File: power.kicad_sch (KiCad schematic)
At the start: 13 parts, among them J2 USB_B_Micro, U2 AP2112K-3.3TRG1, U3 MCP73831T-2ACI/OT

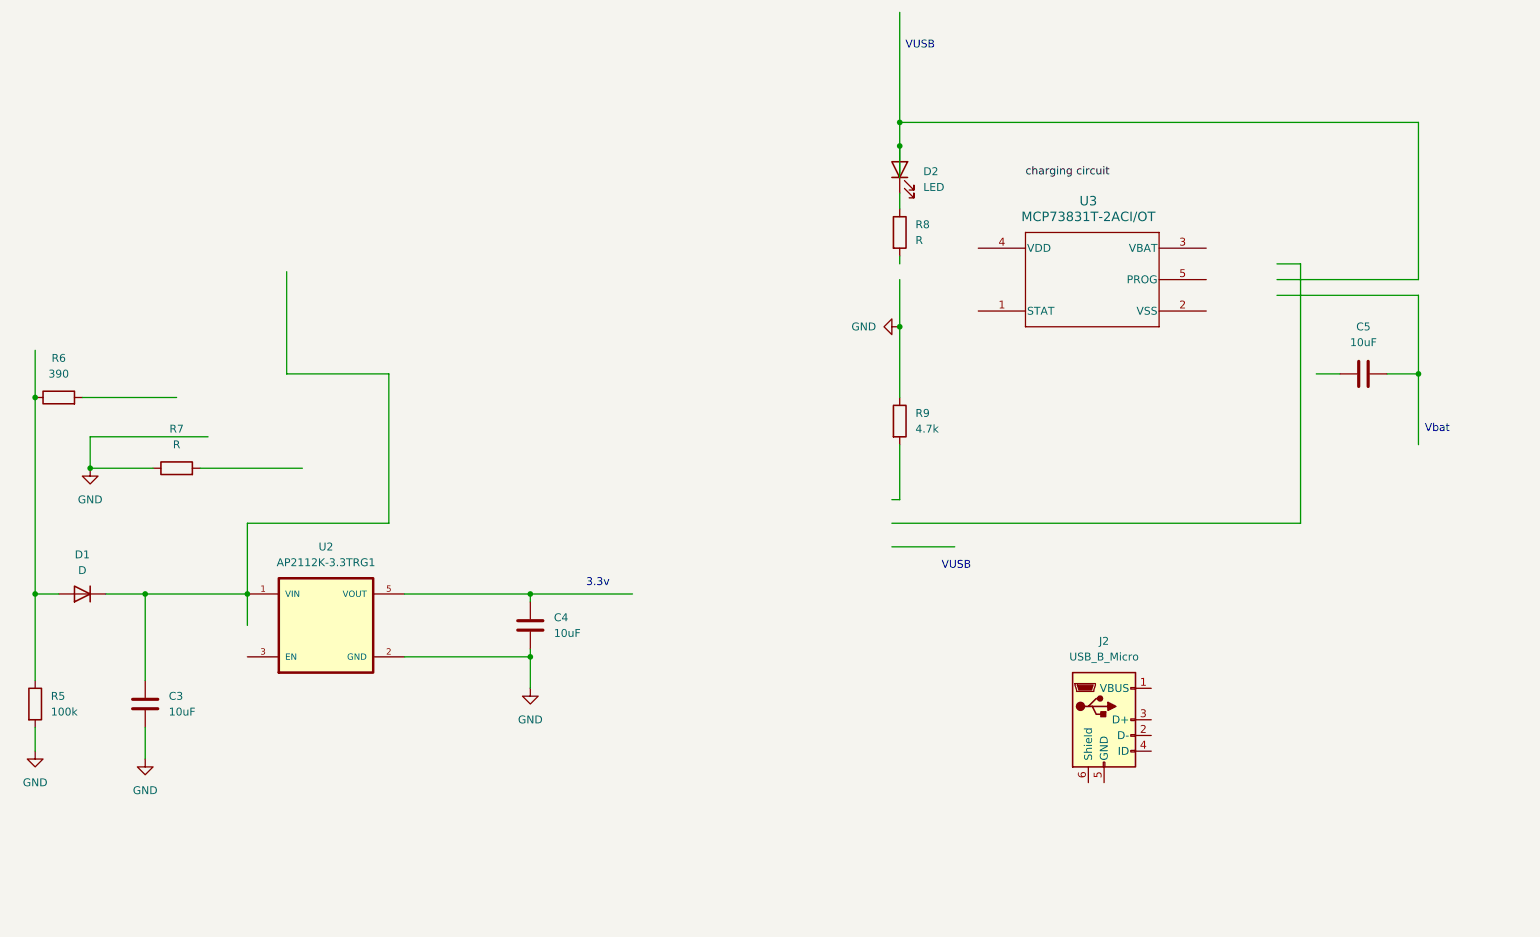
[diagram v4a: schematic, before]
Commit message: update power supply
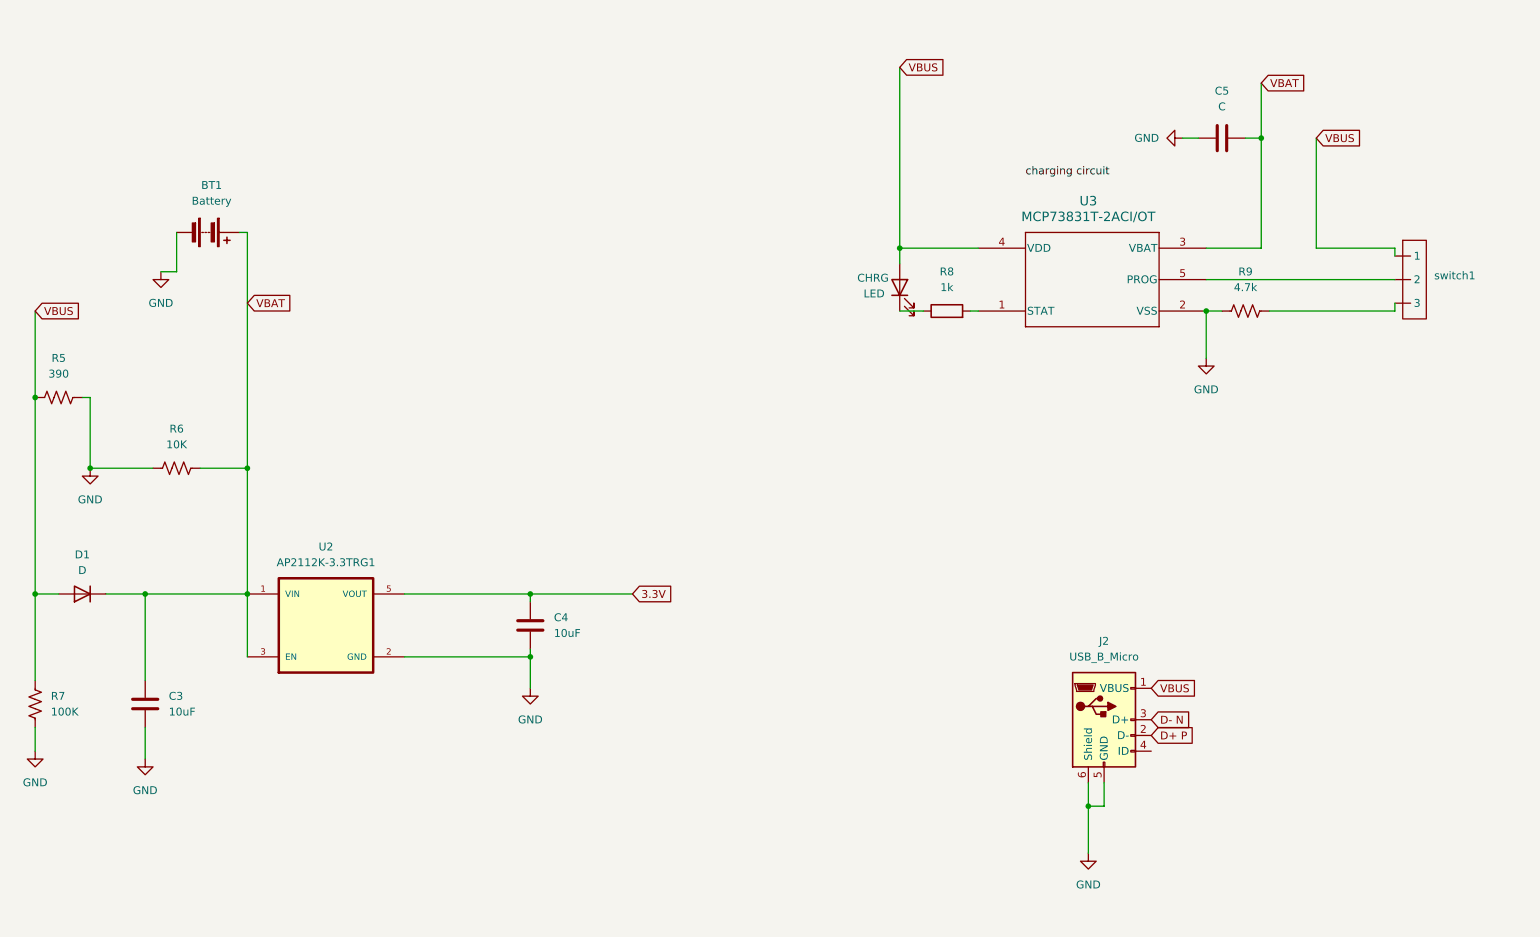
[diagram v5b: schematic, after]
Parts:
- removed C5: 10uF, symbol Device:C
- removed D2: LED, symbol Device:LED
- removed R5: 100k, symbol Device:R
- removed R6: 390, symbol Device:R
- removed R7: R, symbol Device:R
- removed R9: 4.7k, symbol Device:R
- added BT1: Battery, symbol Device:Battery
- added C5: C, Capacitor_SMD:C_0603_1608Metric, symbol uSlime:C
- added CHRG: LED, LED_SMD:LED_0402_1005Metric, symbol uSlime:LED
- added R5: 390, Resistor_SMD:R_0603_1608Metric, symbol uSlime:R_US
- added R6: 10K, Resistor_SMD:R_0603_1608Metric, symbol uSlime:R_US
- added R7: 100K, Resistor_SMD:R_0603_1608Metric, symbol uSlime:R_US
- added R9: 4.7k, Resistor_SMD:R_0603_1608Metric, symbol uSlime:R_US
- added switch1: ~, symbol uSlime:switch
- R8: value R -> 1k
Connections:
- net GND: now also J2.5 (GND), J2.6 (Shield), U3.2 (VSS), BT1.2 (-), C5.1, R5.2, R6.2, R7.2, R9.1
- net 3.3V: now reaches C4.1, U2.5 (VOUT)
- net VBAT: now reaches C3.1, D1.1 (K), U2.1 (VIN)
- net VBAT: now also U2.3 (EN), U3.3 (VBAT), BT1.1 (+), C5.2, R6.1
- net at U3.1 (STAT): now also R8.2
- net VBUS: now reaches U3.4 (VDD)
- net VBUS: now also D1.2 (A), J2.1 (VBUS), CHRG.2 (A), R5.1, R7.1, switch1. (3)
- net at U3.5 (PROG): now also switch1. (3)
- net at R8.1: now also CHRG.1 (K)
- net D+ P: now reaches J2.2 (D-)
- net D- N: now reaches J2.3 (D+)
- new net: R9.2, switch1. (3)
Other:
- note removed: "3.3v"
- note removed: "VUSB"
- note removed: "Vbat"
- moved on the sheet: R8

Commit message: update power
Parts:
- removed R5: 390, Resistor_SMD:R_0603_1608Metric, symbol uSlime:R_US
- removed R6: 10K, Resistor_SMD:R_0603_1608Metric, symbol uSlime:R_US
- removed R7: 100K, Resistor_SMD:R_0603_1608Metric, symbol uSlime:R_US

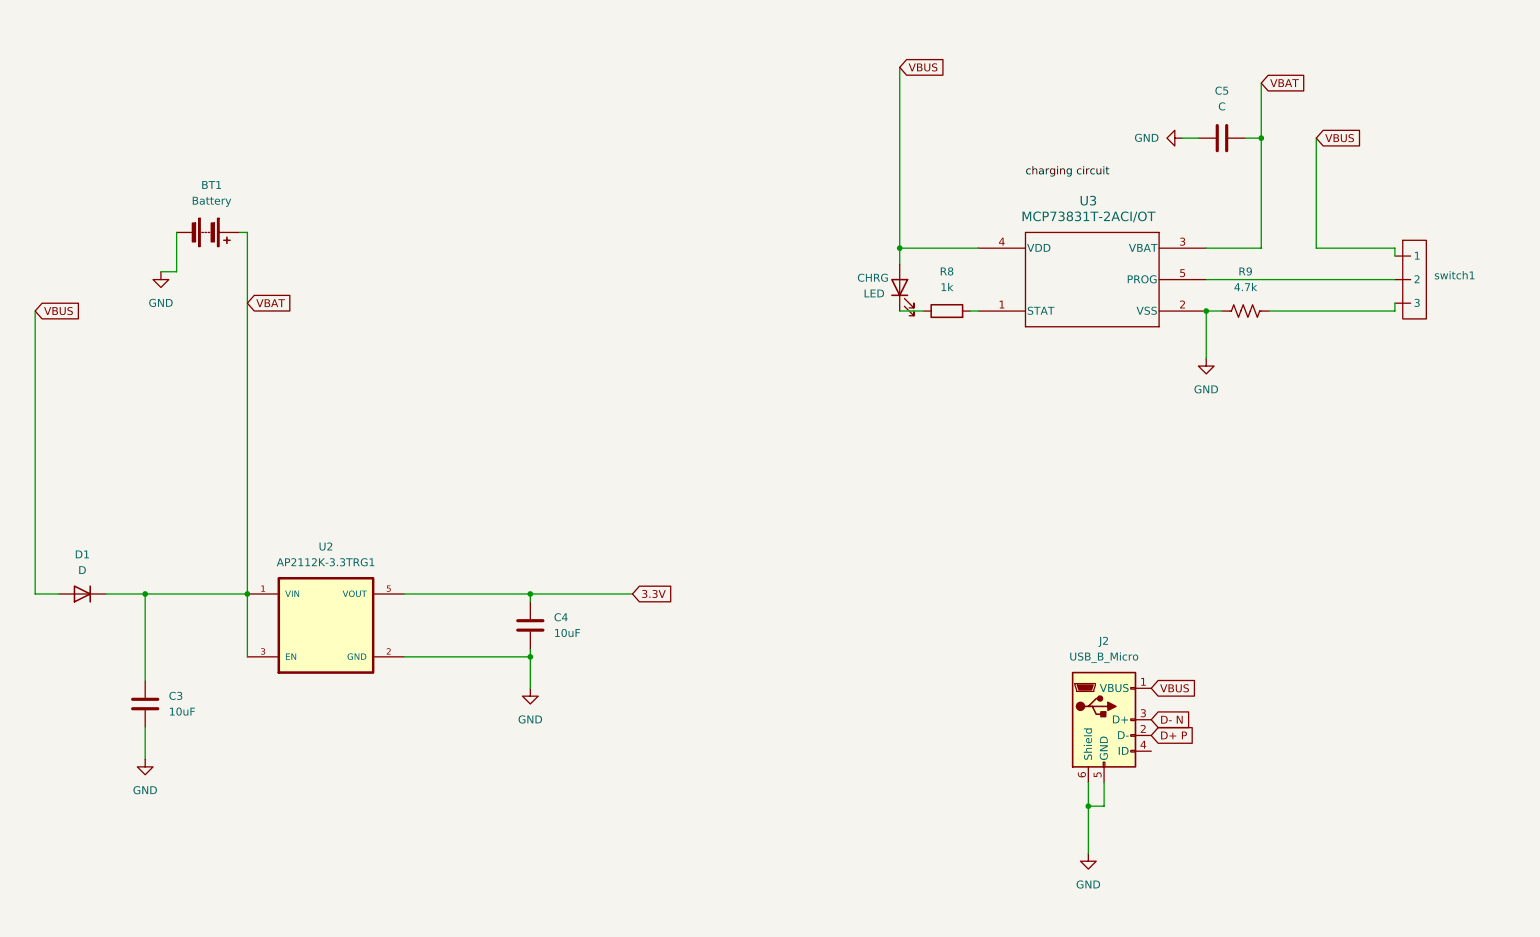
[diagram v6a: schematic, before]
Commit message: Recover old power schematic
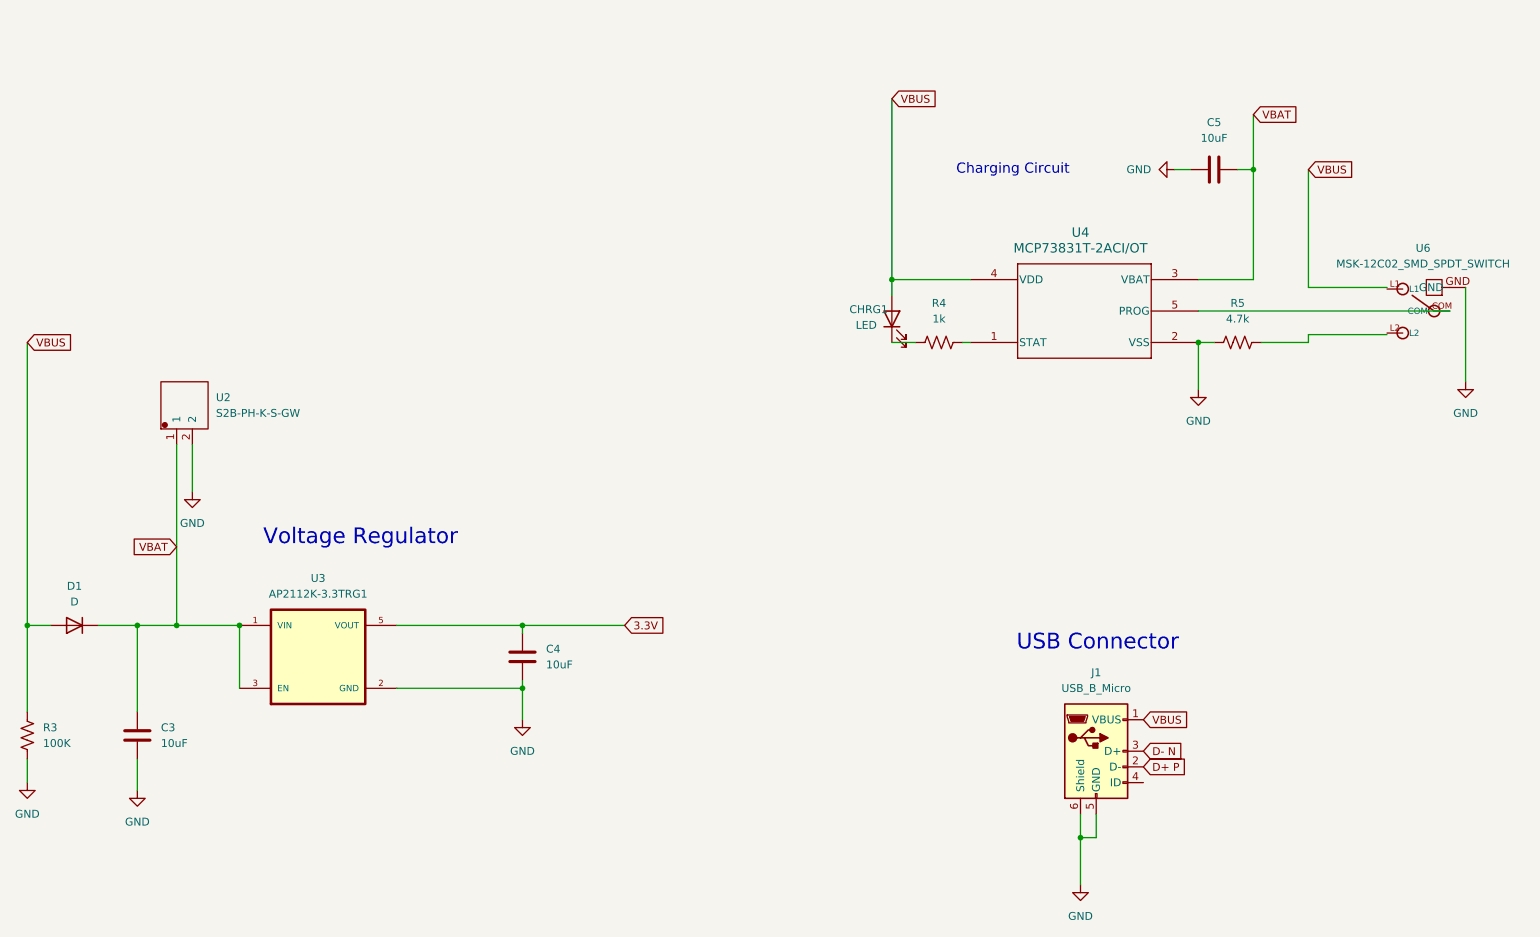
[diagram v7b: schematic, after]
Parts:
- removed BT1: Battery, symbol Device:Battery
- removed C3, C4: 10uF, symbol Device:C
- removed CHRG: LED, LED_SMD:LED_0402_1005Metric, symbol uSlime:LED
- removed D1: D, symbol Device:D
- removed J2: USB_B_Micro, symbol Connector:USB_B_Micro
- removed R8: 1k, symbol Device:R
- removed R9: 4.7k, Resistor_SMD:R_0603_1608Metric, symbol uSlime:R_US
- removed U2: AP2112K-3.3TRG1, uSlime-libs:SOT95P285X140-5N, symbol uSlime:AP2112K-3.3TRG1
- removed U3: MCP73831T-2ACI/OT, uSlime-libs:SOT-23-5_MC_MCH, symbol uSlime:MCP73831T-2ACI_OT
- removed switch1: ~, symbol uSlime:switch
- added C3, C4: 10uF, Capacitor_SMD:C_0603_1608Metric, symbol uSlime:C
- added CHRG1: LED, LED_SMD:LED_0402_1005Metric, symbol uSlime:LED
- added D1: D, Diode_SMD:D_0603_1608Metric, symbol uSlime:D
- added J1: USB_B_Micro, Connector_USB:USB_Micro-B_Amphenol_10103594-0001LF_Horizontal, symbol uSlime:USB_B_Micro
- added R3: 100K, Resistor_SMD:R_0603_1608Metric, symbol uSlime:R_US
- added R4: 1k, Resistor_SMD:R_0603_1608Metric, symbol uSlime:R_US
- added R5: 4.7k, Resistor_SMD:R_0603_1608Metric, symbol uSlime:R_US
- added U2: S2B-PH-K-S-GW, Connector_JST:JST_PH_S2B-PH-K_1x02_P2.00mm_Horizontal, symbol uSlime:S2B-PH-K-S-GW
- added U3: AP2112K-3.3TRG1, uSlime-libs:SOT95P285X140-5N, symbol uSlime:AP2112K-3.3TRG1
- added U4: MCP73831T-2ACI/OT, uSlime-libs:SOT-23-5_MC_MCH, symbol uSlime:MCP73831T-2ACI_OT
- added U6: MSK-12C02_SMD_SPDT_SWITCH, uSlime-libs:SW_PCM12SMTR, symbol uSlime:MSK-12C02_SMD_SPDT_SWITCH
- C5: value C -> 10uF
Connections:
- net 3.3V: now also C4.1, U3.5 (VOUT)
- net D+ P: now also J1.2 (D-)
- net D- N: now also J1.3 (D+)
- net GND: now also C3.2, C4.2, J1.5 (GND), J1.6 (Shield), R3.2, R5.1, U2.2, U3.2 (GND), U4.2 (VSS), U6.GND
- net VBAT: now also C3.1, D1.1 (K), U2.1, U3.1 (VIN), U3.3 (EN), U4.3 (VBAT)
- net VBUS: now also CHRG1.2 (A), D1.2 (A), J1.1 (VBUS), R3.1, U4.4 (VDD)
- new net: CHRG1.1 (K), R4.1
- new net: R4.2, U4.1 (STAT)
- new net: U4.5 (PROG), U6.COM
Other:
- note added: "Charging Circuit"
- note added: "USB Connector"
- note added: "Voltage Regulator"

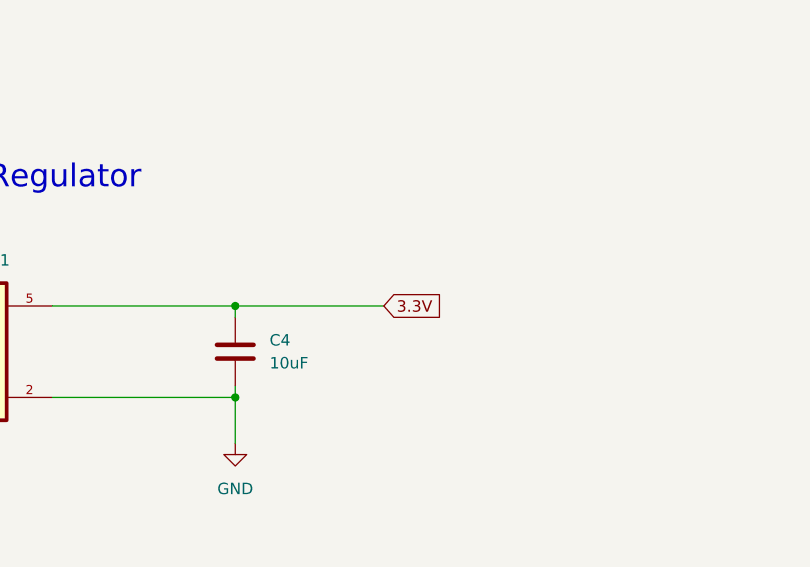
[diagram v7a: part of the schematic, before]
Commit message: Replace ESP32 symbol with right ESP32
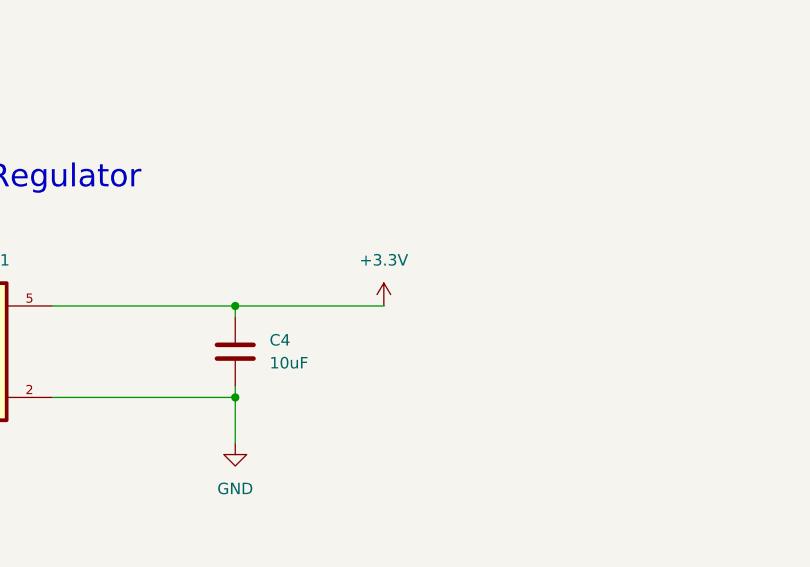
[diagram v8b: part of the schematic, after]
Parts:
- R3, R4, R5: footprint Resistor_SMD:R_0603_1608Metric -> Resistor_SMD:R_0402_1005Metric
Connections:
- net 3.3V renamed +3.3V
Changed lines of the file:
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@@
-		)
-	)
-	(global_label "3.3V"
-		(shape input)
-		(at 129.54 111.76 0)
-		(fields_autoplaced yes)
-		(effects
-			(font
-				(size 1.27 1.27)
-			)
-			(justify left)
-		)
-		(property "Intersheetrefs" "${INTERSHEET_REFS}"
-			(at 136.6376 111.76 0)
-			(effects
-				(font
-					(size 1.27 1.27)
-				)
-				(justify left)
-				(hide yes)
-			)
 		)
 	)
@@
 			)
 		)
-		(property "Footprint" "Resistor_SMD:R_0603_1608Metric"
+		(property "Footprint" "Resistor_SMD:R_0402_1005Metric"
 			(at 180.594 65.024 90)
 			(effects
@@
 	)
 	(symbol
+		(lib_id "power:+3.3V")
+		(at 129.54 111.76 0)
+		(unit 1)
+		(exclude_from_sim no)
+		(in_bom yes)
+		(on_board yes)
+		(dnp no)
+		(fields_autoplaced yes)
+		(property "Reference" "#PWR019"
+			(at 129.54 115.57 0)
+			(effects
+				(font
+					(size 1.27 1.27)
+				)
+				(hide yes)
+			)
+		)
+		(property "Value" "+3.3V"
+			(at 129.54 106.68 0)
+			(effects
+				(font
+					(size 1.27 1.27)
+				)
+			)
+		)
+		(property "Footprint" ""
+			(at 129.54 111.76 0)
+			(effects
+				(font
+					(size 1.27 1.27)
+				)
+				(hide yes)
+			)
+		)
+		(property "Datasheet" ""
+			(at 129.54 111.76 0)
+			(effects
+				(font
+					(size 1.27 1.27)
+				)
+				(hide yes)
+			)
+		)
+		(property "Description" "Power symbol creates a global label with name \"+3.3V\""
+			(at 129.54 111.76 0)
+			(effects
+				(font
+					(size 1.27 1.27)
+				)
+				(hide yes)
+			)
+		)
+		(pin "1"
+		)
+		(instances
+			(project "uSlime"
+				(path "/f32c1c49-f803-4e7c-a530-6db148a7ba36/9141278c-15a6-43aa-8c9d-f1bdf7efadba"
+					(reference "#PWR019")
+					(unit 1)
+				)
+			)
+		)
+	)
+	(symbol
 		(lib_id "uSlime:USB_B_Micro")
 		(at 205.74 132.08 0)
@@
 			)
 		)
-		(property "Footprint" "Resistor_SMD:R_0603_1608Metric"
+		(property "Footprint" "Resistor_SMD:R_0402_1005Metric"
 			(at 34.036 129.794 90)
 			(effects
@@
 			)
 		)
-		(property "Footprint" "Resistor_SMD:R_0603_1608Metric"
+		(property "Footprint" "Resistor_SMD:R_0402_1005Metric"
 			(at 228.854 65.024 90)
 			(effects
